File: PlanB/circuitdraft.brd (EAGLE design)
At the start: 31.2 x 35.4 mm, 19 parts, among them Y1 CY16BPS

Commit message: added tx/rx and moved a few things
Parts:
- added IO: (no value), pinhead:1X03
- moved ISP 2.26 mm to (14.7, 11.9)
- moved C2 0.70 mm to (35.5, 7.00)
- moved Y1 0.54 mm to (27.5, 7.00)
- moved C3 0.40 mm to (19.4, 7.00)
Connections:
- new net RX: IO.1, U$1.20
- new net TX: IO.2, U$1.21
- net GND: now also IO.3
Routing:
- net RX: track 0.00 -> 15.8 mm, vias 0 -> 1
- net TX: track 0.00 -> 12.9 mm, vias 0 -> 1
- net MISO: track 9.96 -> 8.24 mm
- net MOSI: track 12.4 -> 10.9 mm
- net SCK: track 9.23 -> 7.85 mm
- net RST: track 11.3 -> 11.8 mm

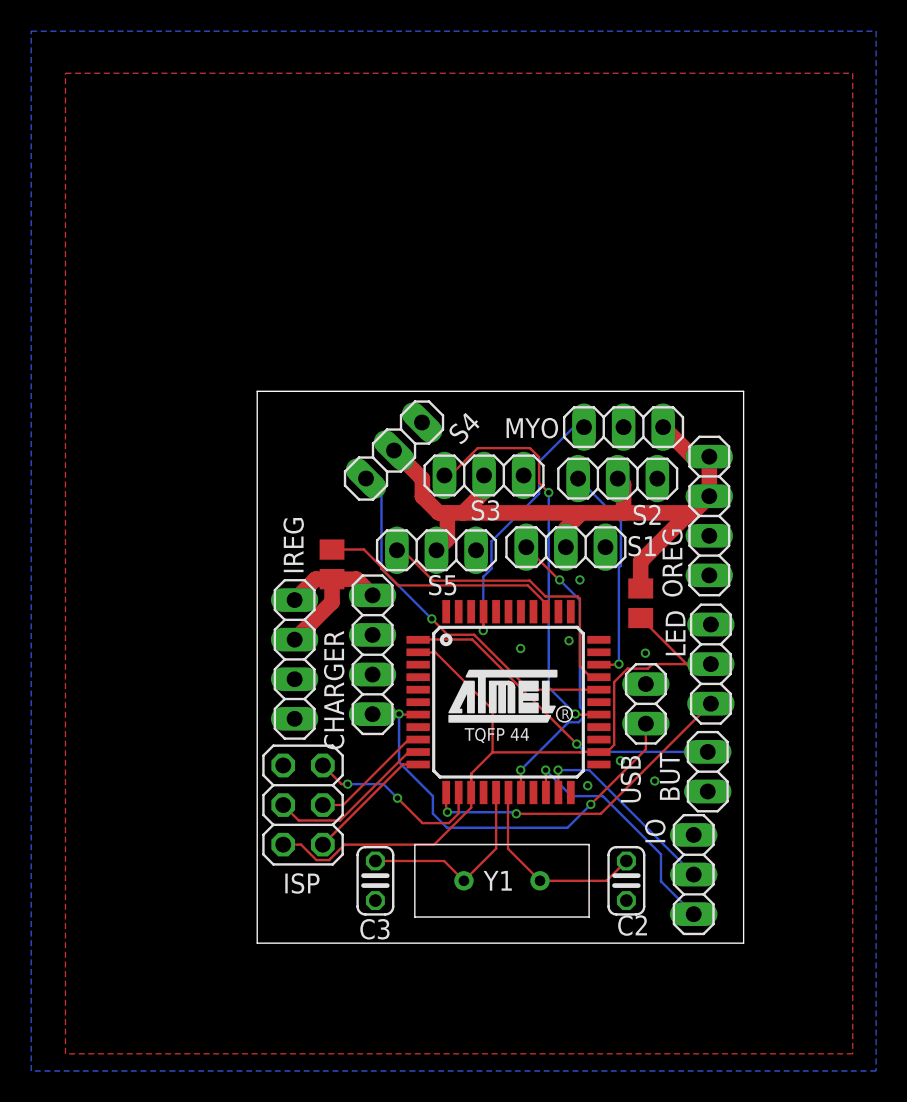
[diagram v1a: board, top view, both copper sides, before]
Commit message: shifted parts to give isp more room
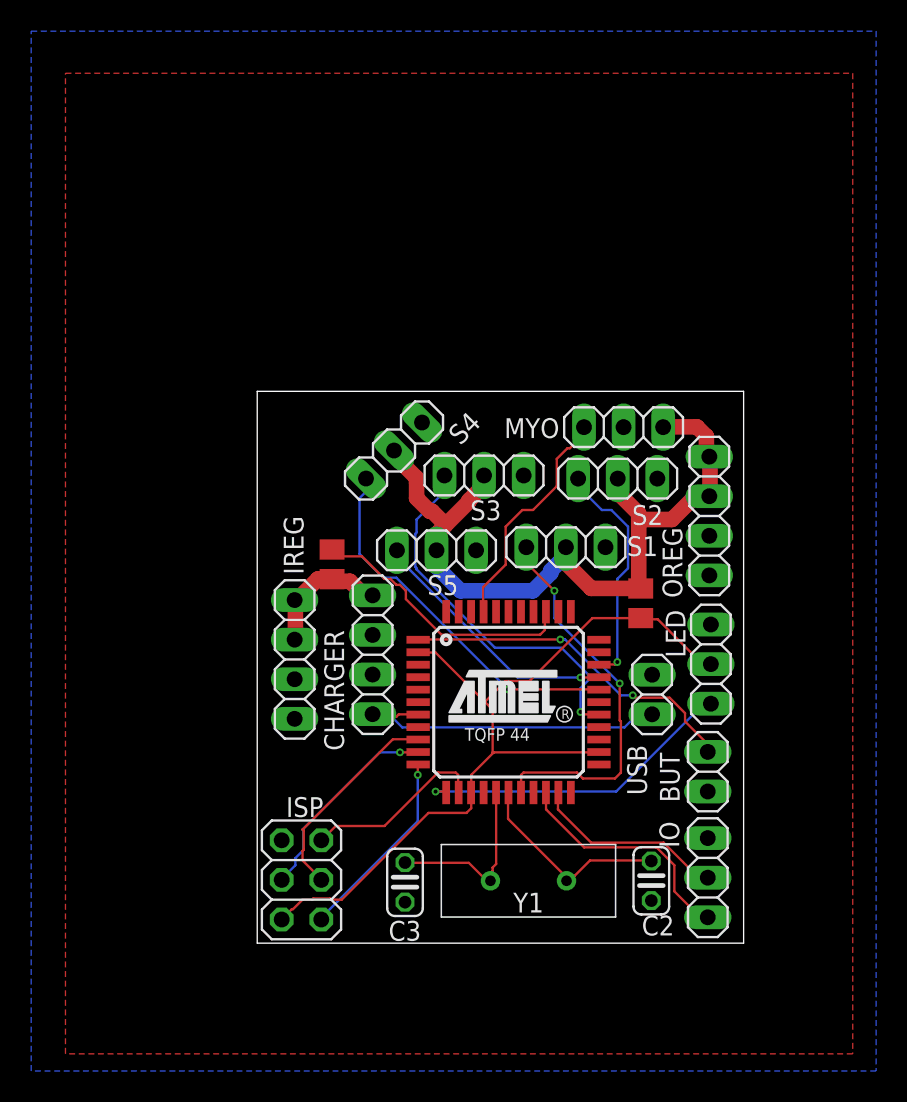
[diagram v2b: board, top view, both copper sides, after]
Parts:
- moved ISP 4.80 mm to (14.6, 7.06)
- moved C3 1.90 mm to (21.3, 6.90)
- moved Y1 1.70 mm to (29.2, 7.00)
- moved C2 1.60 mm to (37.1, 7.00)
- moved IO 0.92 mm to (40.7, 7.20)
- moved USB 0.72 mm to (37.1, 18.9)
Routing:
- net VBUS: track 28.0 -> 21.7 mm, vias 2 -> 0
- net SCK: track 7.85 -> 13.6 mm
- net SIGNAL1: track 19.3 -> 24.9 mm
- net MISO: track 8.24 -> 12.6 mm, vias 0 -> 1
- net BIGPOWER: track 46.2 -> 50.2 mm
- net MOSI: track 10.9 -> 13.3 mm, vias 0 -> 1
- net VBAT: track 10.9 -> 8.54 mm
- net N$1: track 17.3 -> 15.0 mm, vias 1 -> 0
- net SIGNAL5: track 18.9 -> 16.6 mm, vias 0 -> 1
- net N$9: track 15.7 -> 17.6 mm
- net SIGNAL3: track 26.0 -> 24.5 mm, vias 2 -> 1
- net N$5: track 12.6 -> 13.4 mm
- net N$6: track 12.7 -> 12.0 mm
- net SIGNAL4: track 23.4 -> 24.0 mm
- net SIGNAL2: track 14.4 -> 15.0 mm
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
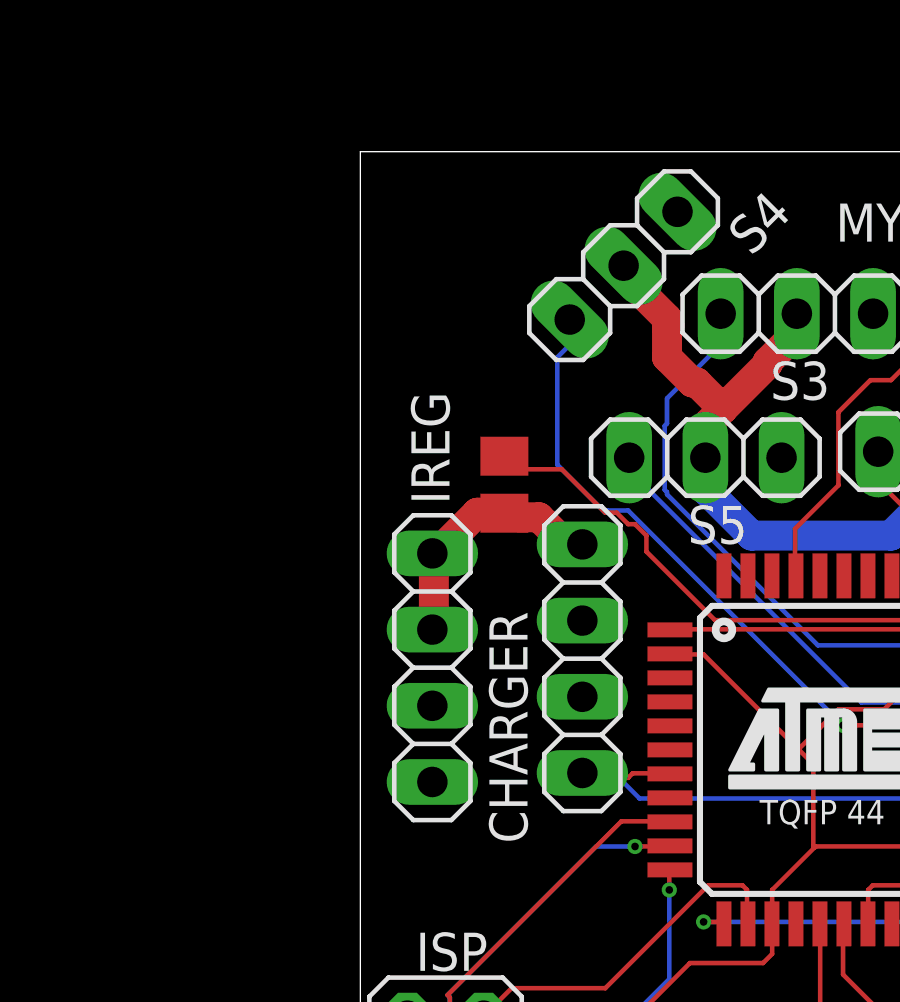
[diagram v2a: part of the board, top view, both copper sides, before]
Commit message: flipped ireg
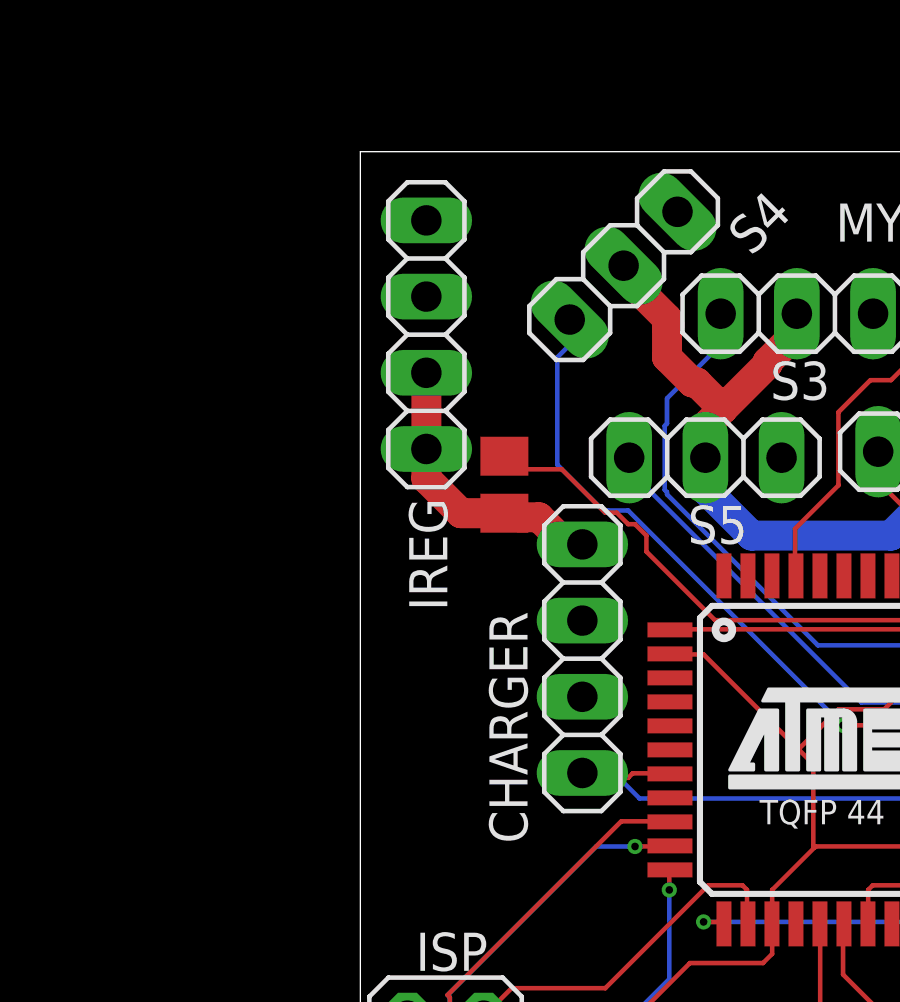
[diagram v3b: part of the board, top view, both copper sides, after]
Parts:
- moved IREG 11.1 mm to (14.0, 32.3), turned to 90 degrees
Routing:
- net VBAT: track 8.54 -> 9.66 mm
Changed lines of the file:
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@@
 <?xml version="1.0" encoding="utf-8"?>
 <!DOCTYPE eagle SYSTEM "eagle.dtd">
-<eagle version="9.5.2">
+<eagle version="9.5.1">
 <drawing>
 <settings>
@@
 <attribute name="NAME" x="29.2" y="5.6" size="1.27" layer="25" align="center"/>
 </element>
-<element name="IREG" library="pinhead" library_urn="urn:adsk.eagle:library:325" package="1X04" package3d_urn="urn:adsk.eagle:package:22407/2" value="" x="14.2" y="21.2" smashed="yes" rot="R270">
-<attribute name="NAME" x="14.7712" y="26.6438" size="1.27" layer="25" ratio="10" rot="R90"/>
-<attribute name="POPULARITY" value="91" x="14.2" y="21.2" size="1.778" layer="27" rot="R270" display="off"/>
-<attribute name="VALUE" x="11.025" y="26.28" size="1.27" layer="27" rot="R270"/>
+<element name="IREG" library="pinhead" library_urn="urn:adsk.eagle:library:325" package="1X04" package3d_urn="urn:adsk.eagle:package:22407/2" value="" x="14" y="32.3" smashed="yes" rot="R90">
+<attribute name="NAME" x="13.4288" y="26.8562" size="1.27" layer="25" ratio="10" rot="R270"/>
+<attribute name="POPULARITY" value="91" x="14" y="32.3" size="1.778" layer="27" rot="R90" display="off"/>
+<attribute name="VALUE" x="17.175" y="27.22" size="1.27" layer="27" rot="R90"/>
 </element>
 <element name="OREG" library="pinhead" library_urn="urn:adsk.eagle:library:325" package="1X04" package3d_urn="urn:adsk.eagle:package:22407/2" value="" x="40.8" y="30.4" smashed="yes" rot="R90">
@@
 <contactref element="IREG" pad="1"/>
 <contactref element="IREG" pad="2"/>
-<wire x1="15.6972" y1="26.3652" x2="16.5354" y2="26.3652" width="1" layer="1"/>
-<wire x1="14.4018" y1="25.0698" x2="15.6972" y2="26.3652" width="1" layer="1"/>
-<wire x1="14.2494" y1="25.0698" x2="14.4018" y2="25.0698" width="1" layer="1"/>
 <wire x1="16.5354" y1="26.3652" x2="16.6" y2="26.35" width="1" layer="1"/>
-<wire x1="14.2494" y1="25.0698" x2="14.2" y2="25.01" width="1" layer="1"/>
-<wire x1="14.2494" y1="24.5364" x2="14.2494" y2="22.479" width="1" layer="1"/>
-<wire x1="14.2494" y1="22.479" x2="14.2" y2="22.47" width="1" layer="1"/>
-<wire x1="14.2494" y1="24.5364" x2="14.2" y2="25.01" width="1" layer="1"/>
 <wire x1="18.5928" y1="25.3746" x2="19.1262" y2="25.3746" width="1" layer="1"/>
 <wire x1="17.7546" y1="26.2128" x2="18.5928" y2="25.3746" width="1" layer="1"/>
@@
 <wire x1="19.1262" y1="25.3746" x2="19.2" y2="25.31" width="1" layer="1"/>
 <wire x1="17.0688" y1="26.2128" x2="16.6" y2="26.35" width="1" layer="1"/>
+<wire x1="16.6" y1="26.35" x2="15.15" y2="26.35" width="1" layer="1"/>
+<wire x1="15.15" y1="26.35" x2="14" y2="27.5" width="1" layer="1"/>
+<wire x1="14" y1="27.5" x2="14" y2="28.49" width="1" layer="1"/>
+<wire x1="14" y1="31.03" x2="14" y2="28.49" width="1" layer="1"/>
 </signal>
 <signal name="N$1">

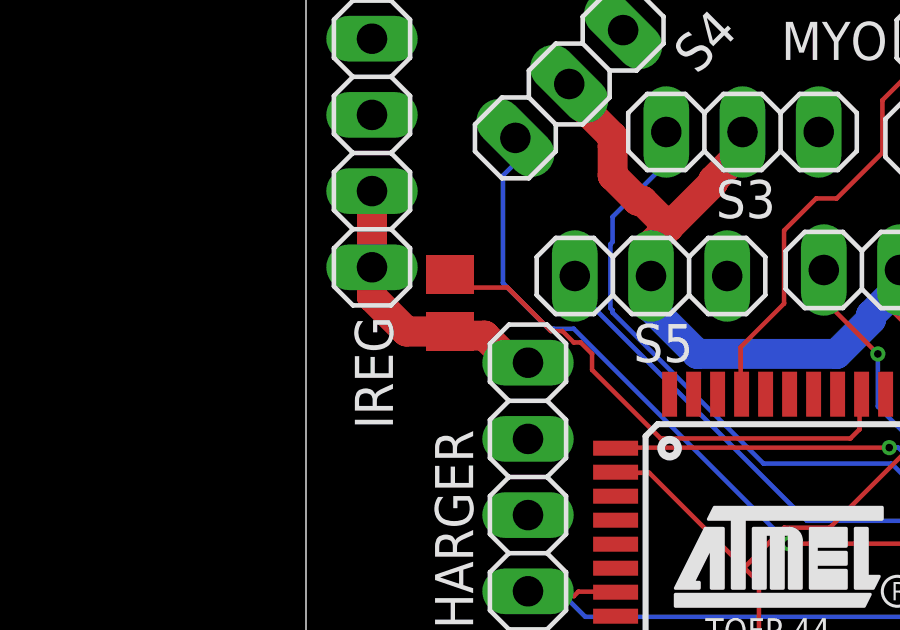
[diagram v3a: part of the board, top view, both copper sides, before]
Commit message: passed drc
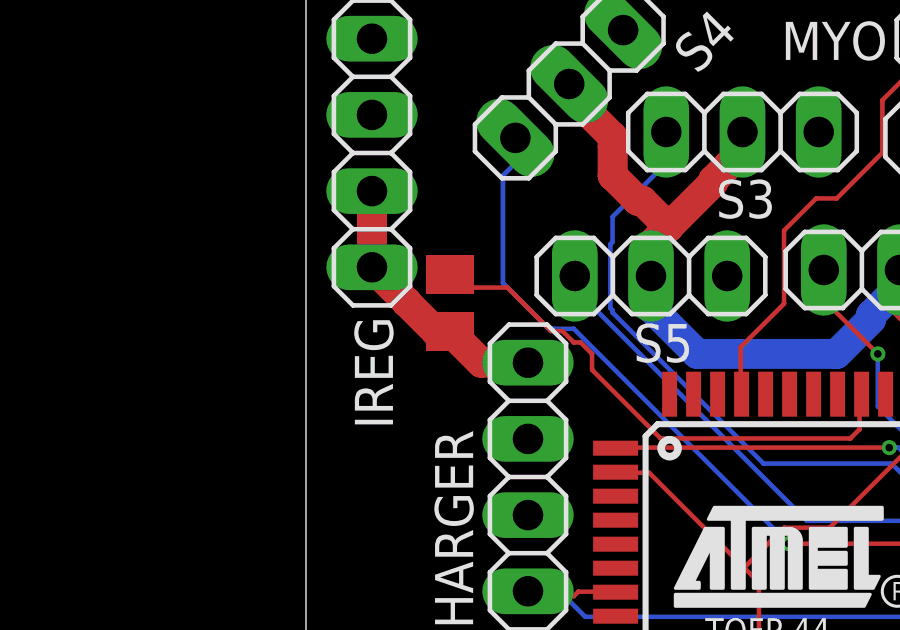
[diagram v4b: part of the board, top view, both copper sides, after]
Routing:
- net VBAT: track 9.66 -> 9.06 mm
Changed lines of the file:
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@@
 <contactref element="IREG" pad="1"/>
 <contactref element="IREG" pad="2"/>
-<wire x1="16.5354" y1="26.3652" x2="16.6" y2="26.35" width="1" layer="1"/>
-<wire x1="18.5928" y1="25.3746" x2="19.1262" y2="25.3746" width="1" layer="1"/>
-<wire x1="17.7546" y1="26.2128" x2="18.5928" y2="25.3746" width="1" layer="1"/>
-<wire x1="17.0688" y1="26.2128" x2="17.7546" y2="26.2128" width="1" layer="1"/>
-<wire x1="19.1262" y1="25.3746" x2="19.2" y2="25.31" width="1" layer="1"/>
-<wire x1="17.0688" y1="26.2128" x2="16.6" y2="26.35" width="1" layer="1"/>
-<wire x1="16.6" y1="26.35" x2="15.15" y2="26.35" width="1" layer="1"/>
-<wire x1="15.15" y1="26.35" x2="14" y2="27.5" width="1" layer="1"/>
-<wire x1="14" y1="27.5" x2="14" y2="28.49" width="1" layer="1"/>
 <wire x1="14" y1="31.03" x2="14" y2="28.49" width="1" layer="1"/>
+<wire x1="14" y1="28.49" x2="15.1476" y2="27.3424" width="1" layer="1"/>
+<wire x1="15.1476" y1="27.3424" x2="15.1476" y2="27.32976875" width="1" layer="1"/>
+<wire x1="15.1476" y1="27.32976875" x2="16.12736875" y2="26.35" width="1" layer="1"/>
+<wire x1="16.12736875" y1="26.35" x2="16.6" y2="26.35" width="1" layer="1"/>
+<wire x1="19.2" y1="25.31" x2="17.64" y2="25.31" width="1" layer="1"/>
+<wire x1="17.64" y1="25.31" x2="16.6" y2="26.35" width="1" layer="1"/>
 </signal>
 <signal name="N$1">
